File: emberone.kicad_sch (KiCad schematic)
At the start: 2 parts, among them J1 Screw Terminal, J2 Screw Terminal

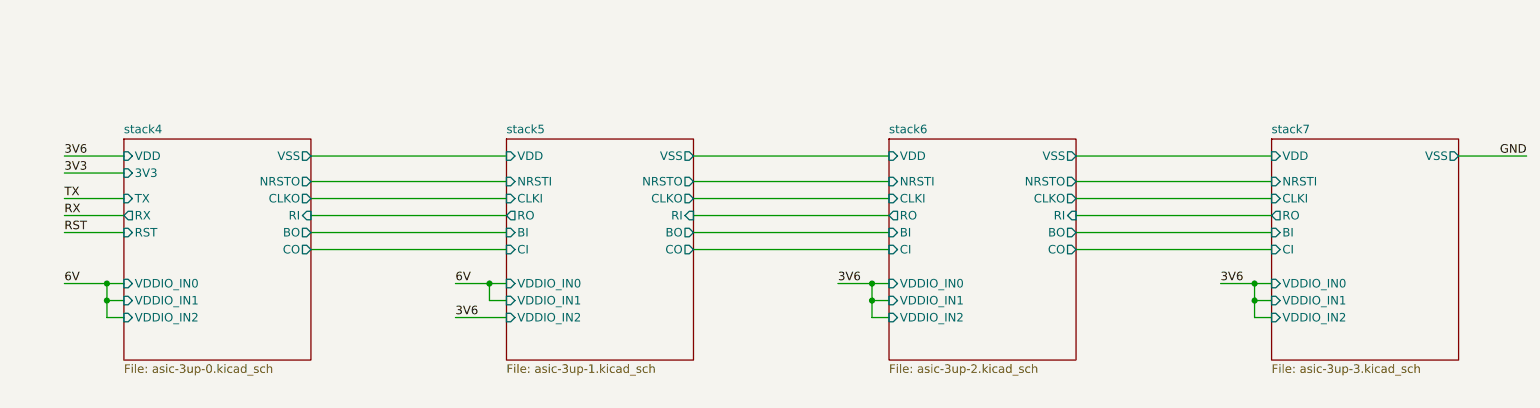
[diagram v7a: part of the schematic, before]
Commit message: forgot that data needs to start with the ASIC that has GND at system GND... reversed everything
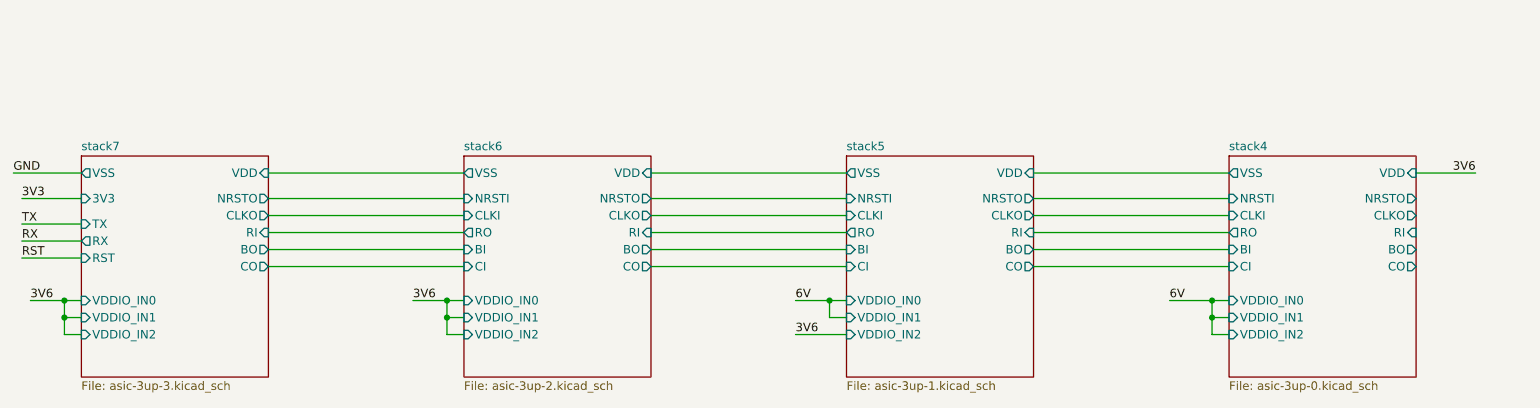
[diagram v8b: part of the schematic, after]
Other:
- sheet stack4 ports: added BI, CI, CLKI, NRSTI, RO; removed 3V3, RST, RX, TX
- sheet stack7 ports: added 3V3, BO, CLKO, CO, NRSTO, RI, RST, RX, TX; removed BI, CI, CLKI, NRSTI, RO
